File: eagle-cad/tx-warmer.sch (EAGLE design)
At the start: 22 parts

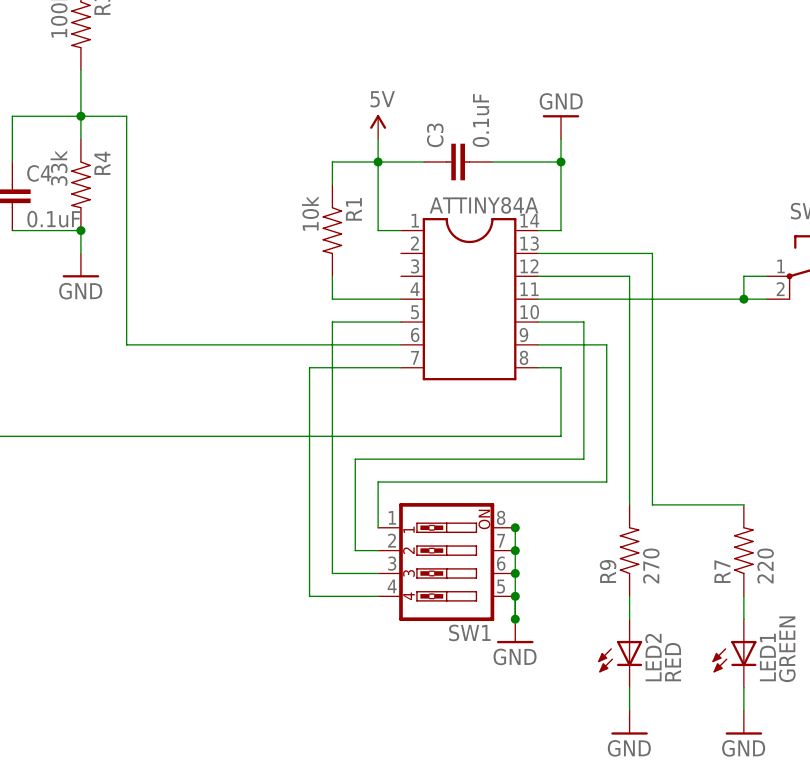
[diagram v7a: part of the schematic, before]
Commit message: Changed 4P-switch to 6P-switch to utilize all inputs
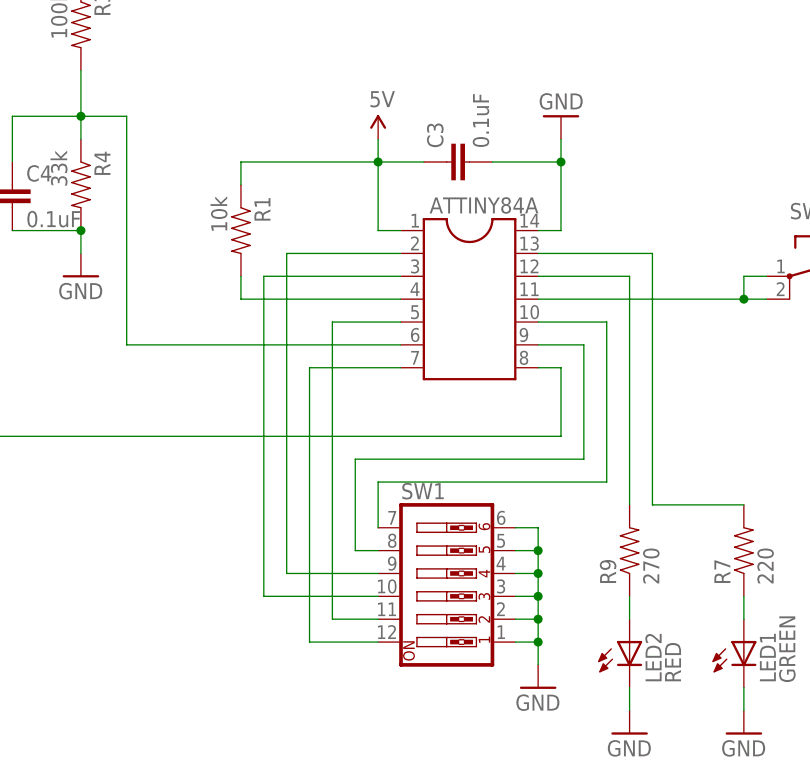
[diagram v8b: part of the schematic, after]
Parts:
- SW1: device special:SW_DIP-4 -> special:SW_DIP-6
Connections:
- new net N$21: ATTINY84A.3, SW1.10
- new net N$3: ATTINY84A.2, SW1.9
- net GND: now also SW1.1, SW1.2, SW1.3, SW1.4; no longer SW1.7, SW1.8
- net N$1: now also SW1.12; no longer SW1.4
- net N$2: now also SW1.11; no longer SW1.3
- net N$20: now also ATTINY84A.10, SW1.7; no longer ATTINY84A.9, SW1.1
- net N$5: now also ATTINY84A.9, SW1.8; no longer ATTINY84A.10, SW1.2
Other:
- moved on the sheet: R1
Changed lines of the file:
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@@
 <part name="H-" library="SparkFun-Connectors" deviceset="M01" device="PTH_2MM"/>
 <part name="LP2950" library="SparkFun-Connectors" deviceset="M03" device="1X03_NO_SILK"/>
-<part name="SW1" library="special" deviceset="SW_DIP-4" device=""/>
 <part name="GND4" library="SparkFun-Aesthetics" deviceset="GND" device=""/>
 <part name="C2" library="SparkFun-Passives" deviceset="CAP" device="PTH1" value="2.2uF"/>
 <part name="C1" library="SparkFun-Passives" deviceset="CAP" device="PTH1" value="2.2uF"/>
+<part name="SW1" library="special" deviceset="SW_DIP-6" device=""/>
 </parts>
 <sheets>
@@
 <instance part="C4" gate="G$1" x="60.96" y="63.5"/>
 <instance part="C3" gate="G$1" x="111.76" y="68.58" rot="R90"/>
-<instance part="R1" gate="G$1" x="96.52" y="60.96" rot="R270"/>
+<instance part="R1" gate="G$1" x="86.36" y="60.96" rot="R270"/>
 <instance part="B+" gate="G$1" x="-5.08" y="78.74"/>
 <instance part="H+" gate="G$1" x="-5.08" y="71.12"/>
@@
 <instance part="H-" gate="G$1" x="-5.08" y="33.02"/>
 <instance part="LP2950" gate="G$1" x="35.56" y="78.74" rot="R270"/>
-<instance part="SW1" gate="A" x="109.22" y="22.86" rot="R180"/>
-<instance part="GND4" gate="1" x="116.84" y="15.24"/>
+<instance part="GND4" gate="1" x="119.38" y="10.16"/>
 <instance part="C2" gate="G$1" x="20.32" y="63.5"/>
 <instance part="C1" gate="G$1" x="43.18" y="63.5"/>
+<instance part="SW1" gate="A" x="109.22" y="22.86"/>
 </instances>
 <busses>
@@
 </segment>
 <segment>
-<pinref part="SW1" gate="A" pin="8"/>
-<pinref part="SW1" gate="A" pin="7"/>
-<wire x1="116.84" y1="27.94" x2="116.84" y2="25.4" width="0.1524" layer="91"/>
 <pinref part="SW1" gate="A" pin="6"/>
-<wire x1="116.84" y1="25.4" x2="116.84" y2="22.86" width="0.1524" layer="91"/>
+<wire x1="116.84" y1="27.94" x2="119.38" y2="27.94" width="0.1524" layer="91"/>
+<wire x1="119.38" y1="27.94" x2="119.38" y2="25.4" width="0.1524" layer="91"/>
+<pinref part="SW1" gate="A" pin="1"/>
+<wire x1="119.38" y1="25.4" x2="119.38" y2="22.86" width="0.1524" layer="91"/>
+<wire x1="119.38" y1="22.86" x2="119.38" y2="20.32" width="0.1524" layer="91"/>
+<wire x1="119.38" y1="20.32" x2="119.38" y2="17.78" width="0.1524" layer="91"/>
+<wire x1="119.38" y1="17.78" x2="119.38" y2="15.24" width="0.1524" layer="91"/>
+<wire x1="119.38" y1="15.24" x2="119.38" y2="12.7" width="0.1524" layer="91"/>
+<wire x1="116.84" y1="15.24" x2="119.38" y2="15.24" width="0.1524" layer="91"/>
+<pinref part="SW1" gate="A" pin="2"/>
+<wire x1="116.84" y1="17.78" x2="119.38" y2="17.78" width="0.1524" layer="91"/>
+<pinref part="SW1" gate="A" pin="3"/>
+<wire x1="116.84" y1="20.32" x2="119.38" y2="20.32" width="0.1524" layer="91"/>
+<pinref part="SW1" gate="A" pin="4"/>
+<wire x1="116.84" y1="22.86" x2="119.38" y2="22.86" width="0.1524" layer="91"/>
 <pinref part="SW1" gate="A" pin="5"/>
-<wire x1="116.84" y1="22.86" x2="116.84" y2="20.32" width="0.1524" layer="91"/>
+<wire x1="116.84" y1="25.4" x2="119.38" y2="25.4" width="0.1524" layer="91"/>
 <pinref part="GND4" gate="1" pin="GND"/>
-<wire x1="116.84" y1="20.32" x2="116.84" y2="17.78" width="0.1524" layer="91"/>
-<wire x1="116.84" y1="17.78" x2="116.84" y2="20.32" width="0.1524" layer="91"/>
-<junction x="116.84" y="17.78"/>
-<junction x="116.84" y="27.94"/>
-<junction x="116.84" y="25.4"/>
-<junction x="116.84" y="22.86"/>
-<junction x="116.84" y="20.32"/>
+<junction x="119.38" y="15.24"/>
+<junction x="119.38" y="17.78"/>
+<junction x="119.38" y="20.32"/>
+<junction x="119.38" y="22.86"/>
+<junction x="119.38" y="25.4"/>
 </segment>
 </net>
@@
 <pinref part="C3" gate="G$1" pin="1"/>
 <pinref part="R1" gate="G$1" pin="1"/>
-<wire x1="96.52" y1="66.04" x2="96.52" y2="68.58" width="0.1524" layer="91"/>
-<wire x1="96.52" y1="68.58" x2="101.6" y2="68.58" width="0.1524" layer="91"/>
+<wire x1="86.36" y1="66.04" x2="86.36" y2="68.58" width="0.1524" layer="91"/>
+<wire x1="86.36" y1="68.58" x2="101.6" y2="68.58" width="0.1524" layer="91"/>
 </segment>
 <segment>
@@
 <pinref part="ATTINY84A" gate="G$1" pin="4"/>
 <pinref part="R1" gate="G$1" pin="2"/>
-<wire x1="104.14" y1="53.34" x2="96.52" y2="53.34" width="0.1524" layer="91"/>
-<wire x1="96.52" y1="53.34" x2="96.52" y2="55.88" width="0.1524" layer="91"/>
+<wire x1="104.14" y1="53.34" x2="86.36" y2="53.34" width="0.1524" layer="91"/>
+<wire x1="86.36" y1="53.34" x2="86.36" y2="55.88" width="0.1524" layer="91"/>
 </segment>
 </net>
@@
 <net name="N$1" class="0">
 <segment>
-<wire x1="93.98" y1="20.32" x2="93.98" y2="45.72" width="0.1524" layer="91"/>
+<wire x1="93.98" y1="15.24" x2="93.98" y2="45.72" width="0.1524" layer="91"/>
 <pinref part="ATTINY84A" gate="G$1" pin="7"/>
 <wire x1="93.98" y1="45.72" x2="104.14" y2="45.72" width="0.1524" layer="91"/>
-<pinref part="SW1" gate="A" pin="4"/>
-<wire x1="93.98" y1="20.32" x2="101.6" y2="20.32" width="0.1524" layer="91"/>
+<pinref part="SW1" gate="A" pin="12"/>
+<wire x1="93.98" y1="15.24" x2="101.6" y2="15.24" width="0.1524" layer="91"/>
 </segment>
 </net>
 <net name="N$2" class="0">
 <segment>
-<wire x1="96.52" y1="22.86" x2="96.52" y2="50.8" width="0.1524" layer="91"/>
+<wire x1="96.52" y1="17.78" x2="96.52" y2="50.8" width="0.1524" layer="91"/>
 <pinref part="ATTINY84A" gate="G$1" pin="5"/>
 <wire x1="96.52" y1="50.8" x2="104.14" y2="50.8" width="0.1524" layer="91"/>
-<pinref part="SW1" gate="A" pin="3"/>
-<wire x1="96.52" y1="22.86" x2="101.6" y2="22.86" width="0.1524" layer="91"/>
+<pinref part="SW1" gate="A" pin="11"/>
+<wire x1="96.52" y1="17.78" x2="101.6" y2="17.78" width="0.1524" layer="91"/>
 </segment>
 </net>
 <net name="N$5" class="0">
 <segment>
-<wire x1="124.46" y1="50.8" x2="124.46" y2="35.56" width="0.1524" layer="91"/>
 <wire x1="124.46" y1="35.56" x2="99.06" y2="35.56" width="0.1524" layer="91"/>
+<wire x1="99.06" y1="35.56" x2="99.06" y2="25.4" width="0.1524" layer="91"/>
+<wire x1="99.06" y1="25.4" x2="101.6" y2="25.4" width="0.1524" layer="91"/>
+<pinref part="SW1" gate="A" pin="8"/>
+<pinref part="ATTINY84A" gate="G$1" pin="9"/>
+<wire x1="119.38" y1="48.26" x2="124.46" y2="48.26" width="0.1524" layer="91"/>
+<wire x1="124.46" y1="48.26" x2="124.46" y2="35.56" width="0.1524" layer="91"/>
+</segment>
+</net>
+<net name="N$20" class="0">
+<segment>
+<wire x1="127" y1="33.02" x2="101.6" y2="33.02" width="0.1524" layer="91"/>
+<wire x1="127" y1="33.02" x2="127" y2="50.8" width="0.1524" layer="91"/>
+<wire x1="101.6" y1="33.02" x2="101.6" y2="27.94" width="0.1524" layer="91"/>
+<pinref part="SW1" gate="A" pin="7"/>
 <pinref part="ATTINY84A" gate="G$1" pin="10"/>
-<wire x1="124.46" y1="50.8" x2="119.38" y2="50.8" width="0.1524" layer="91"/>
-<wire x1="99.06" y1="35.56" x2="99.06" y2="25.4" width="0.1524" layer="91"/>
-<pinref part="SW1" gate="A" pin="2"/>
-<wire x1="99.06" y1="25.4" x2="101.6" y2="25.4" width="0.1524" layer="91"/>
-</segment>
-</net>
-<net name="N$20" class="0">
-<segment>
-<wire x1="127" y1="33.02" x2="101.6" y2="33.02" width="0.1524" layer="91"/>
-<wire x1="127" y1="33.02" x2="127" y2="48.26" width="0.1524" layer="91"/>
-<pinref part="ATTINY84A" gate="G$1" pin="9"/>
-<wire x1="127" y1="48.26" x2="119.38" y2="48.26" width="0.1524" layer="91"/>
-<wire x1="101.6" y1="33.02" x2="101.6" y2="27.94" width="0.1524" layer="91"/>
-<pinref part="SW1" gate="A" pin="1"/>
-</segment>
-</net>
+<wire x1="127" y1="50.8" x2="119.38" y2="50.8" width="0.1524" layer="91"/>
+</segment>
+</net>
+<net name="N$3" class="0">
+<segment>
+<pinref part="ATTINY84A" gate="G$1" pin="2"/>
+<wire x1="104.14" y1="58.42" x2="91.44" y2="58.42" width="0.1524" layer="91"/>
+<wire x1="91.44" y1="58.42" x2="91.44" y2="22.86" width="0.1524" layer="91"/>
+<pinref part="SW1" gate="A" pin="9"/>
+<wire x1="91.44" y1="22.86" x2="101.6" y2="22.86" width="0.1524" layer="91"/>
+</segment>
+</net>
+<net name="N$21" class="0">
+<segment>
+<pinref part="ATTINY84A" gate="G$1" pin="3"/>
+<wire x1="104.14" y1="55.88" x2="88.9" y2="55.88" width="0.1524" layer="91"/>
+<wire x1="88.9" y1="55.88" x2="88.9" y2="20.32" width="0.1524" layer="91"/>
+<pinref part="SW1" gate="A" pin="10"/>
+<wire x1="88.9" y1="20.32" x2="101.6" y2="20.32" width="0.1524" layer="91"/>
+</segment>
+</net>
